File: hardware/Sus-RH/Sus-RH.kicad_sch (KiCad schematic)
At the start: 36 parts, among them J1 MX150_02x06_Vertical, J2 53307-2471, J3 Conn_01x03, J5 Conn_01x06, U1 TLV9002QDRQ1, U2 LDO40LPURY

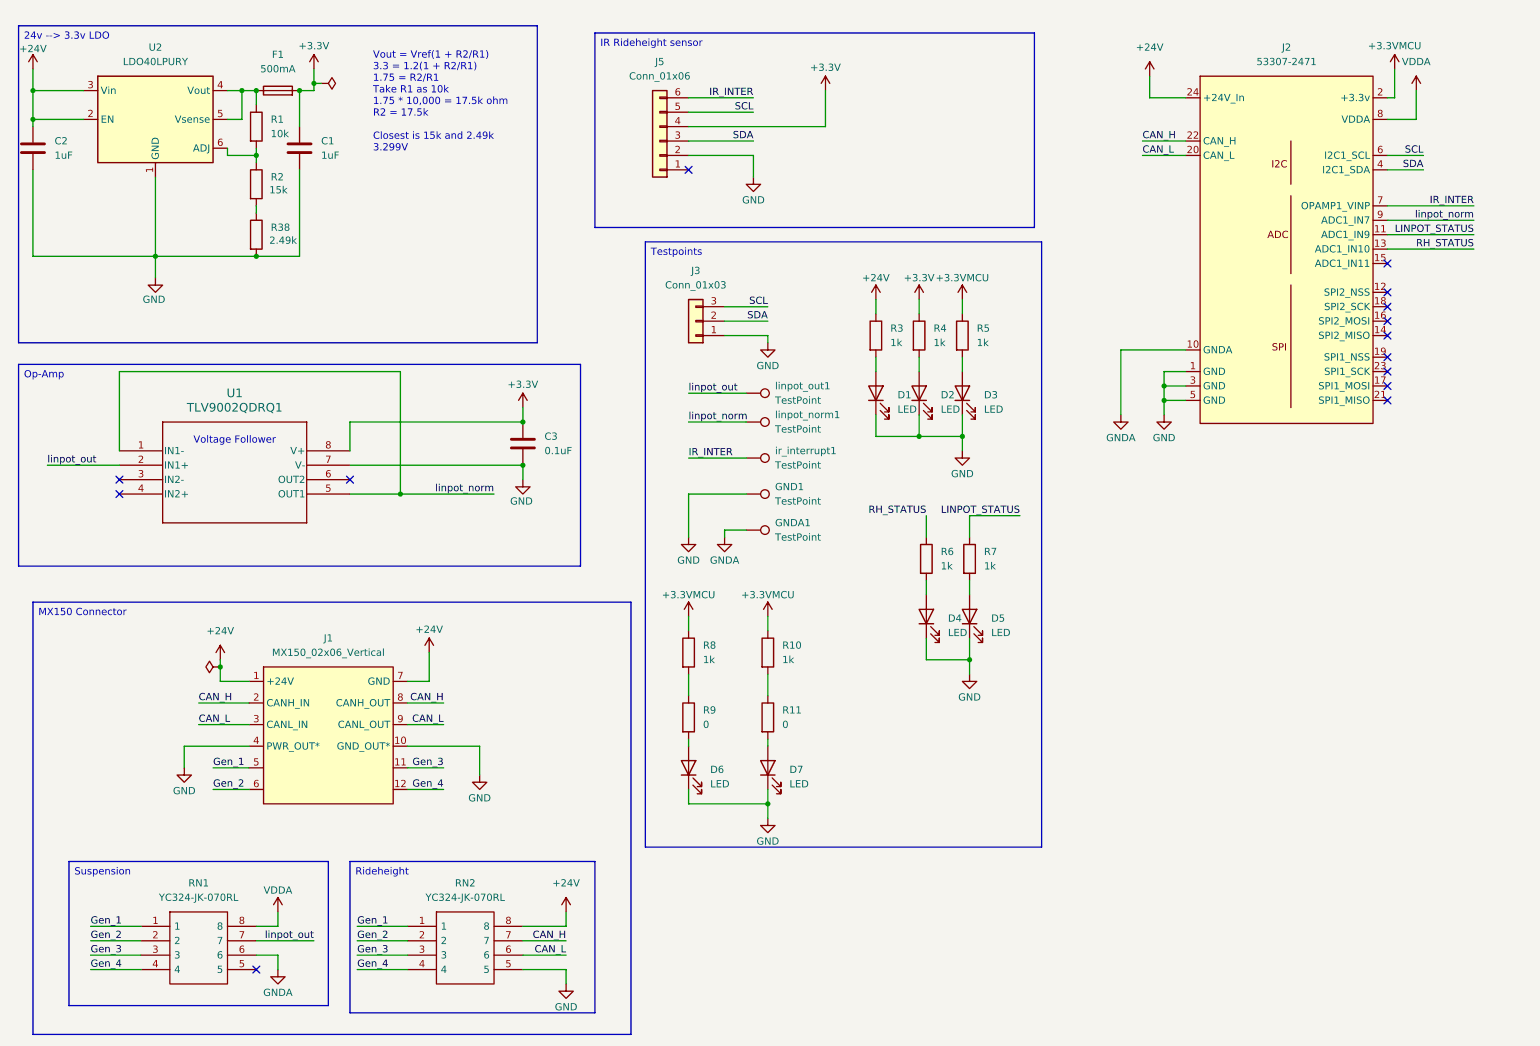
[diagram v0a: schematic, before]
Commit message: small changes, cubemx needs checking
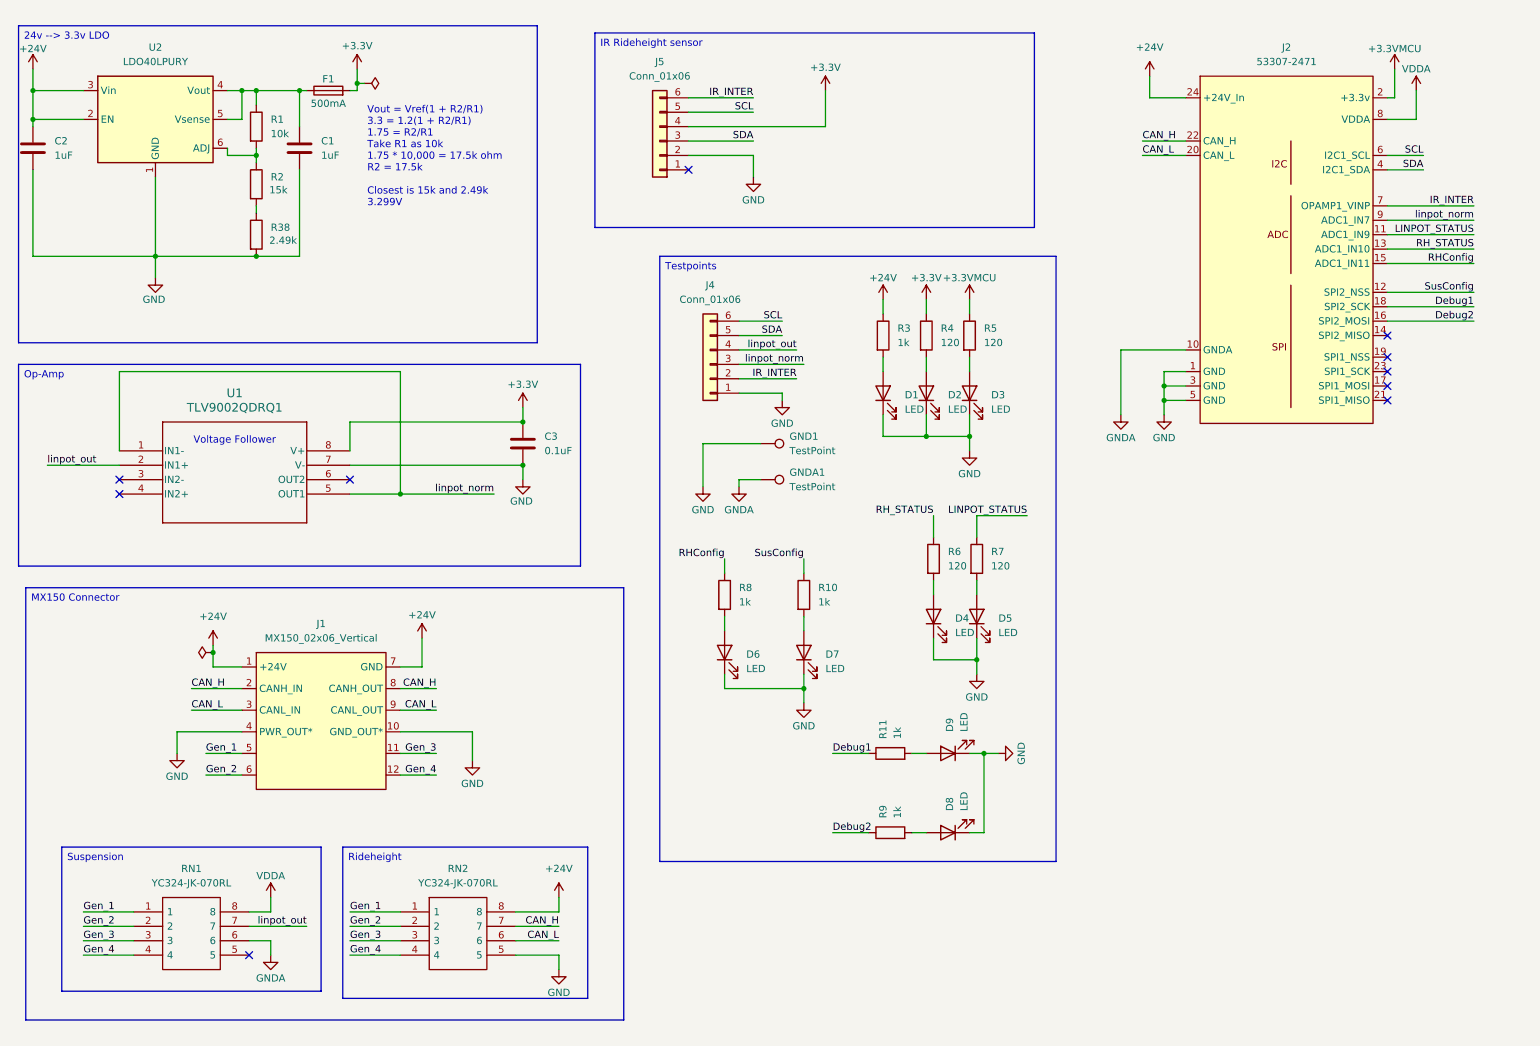
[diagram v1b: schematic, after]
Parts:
- removed J3: Conn_01x03, symbol Connector_Generic:Conn_01x03
- removed ir_interrupt1, linpot_norm1, linpot_out1: TestPoint, symbol Connector:TestPoint
- added D8, D9: LED, LED_SMD:LED_0603_1608Metric_Pad1.05x0.95mm_HandSolder, symbol Device:LED
- added J4: Conn_01x06, symbol Connector_Generic:Conn_01x06
- C3: footprint (none) -> Capacitor_SMD:C_0603_1608Metric_Pad1.08x0.95mm_HandSolder; P/N (none) -> MLASH168SB7104KTNA01
- D1, D2, D3, D4, D5, D6, D7: footprint (none) -> LED_SMD:LED_0603_1608Metric_Pad1.05x0.95mm_HandSolder; P/N (none) -> NCD0603R1
- GND1, GNDA1: footprint (none) -> TestPoint:TestPoint_Pad_1.0x1.0mm
- R10, R3, R8: footprint (none) -> Resistor_SMD:R_0603_1608Metric_Pad0.98x0.95mm_HandSolder; P/N (none) -> CRCW06031K00FKEI
- R11, R9: value 0 -> 1k; footprint (none) -> Resistor_SMD:R_0603_1608Metric_Pad0.98x0.95mm_HandSolder; P/N (none) -> CRCW06031K00FKEI
- R4, R5, R6, R7: value 1k -> 120; footprint (none) -> Resistor_SMD:R_0603_1608Metric_Pad0.98x0.95mm_HandSolder; P/N (none) -> CRCW06031K00FKEI
- RN1, RN2: footprint YC324JK07220RL -> 4pinRes:YC324JK07220RL; P/N (none) -> 603-YC324-JK-070RL
- U1: footprint SOIC8_D_TEX -> footprints:SOIC8_D_TEX; P/N (none) -> 595-TLV9002QDRQ1
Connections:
- net +3.3V: no longer C1.1
- net +3.3VMCU: no longer R10.1, R8.1
- net GND: now also D8.1 (K), D9.1 (K), J4.1 (Pin_1)
- net IR_INTER: now also J4.2 (Pin_2)
- net SCL: now also J4.6 (Pin_6)
- net SDA: now also J4.5 (Pin_5)
- net linpot_norm: now also J4.3 (Pin_3)
- net linpot_out: now also J4.4 (Pin_4)
- net at F1.1, R1.1, U2.4 (Vout)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: now also C1.1
- net at R8.2: now also D6.2 (A); no longer R9.1
- net at R9.2: now also D8.2 (A); no longer D6.2 (A)
- net at R10.2: now also D7.2 (A); no longer R11.1
- net at R11.2: now also D9.2 (A); no longer D7.2 (A)
- net SusConfig: now reaches J2.12 (SPI2_NSS)
- net SusConfig: now also R10.1
- net RHConfig: now reaches J2.15 (ADC1_IN11)
- net RHConfig: now also R8.1
- net Debug2: now reaches J2.16 (SPI2_MOSI)
- net Debug2: now also R9.1
- net Debug1: now reaches J2.18 (SPI2_SCK)
- net Debug1: now also R11.1
- no-connect marks 14 -> 10
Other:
- moved on the sheet: D1, D2, D3, D4, D5, D6, D7, F1, GND1, GNDA1, J1, R10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

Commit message: finished layout
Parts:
- J4: footprint (none) -> Connector_PinHeader_2.54mm:PinHeader_1x06_P2.54mm_Vertical
- J5: footprint Connector_Molex:Molex_Nano-Fit_105310-xx06_2x03_P2.50mm_Vertical -> Connector_Molex:Molex_Nano-Fit_105314-xx06_2x03_P2.50mm_Horizontal
- R3: value 1k -> 4.7k
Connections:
- net +24V: now also RN2.5; no longer RN2.8
- net GND: now also RN2.8; no longer RN2.5
- net Gen_1: now also RN2.4; no longer RN2.1
- net Gen_2: now also RN2.3; no longer RN2.2
- net Gen_3: now also RN2.2; no longer RN2.3
- net Gen_4: now also RN2.1; no longer RN2.4
- net CAN_H renamed CAN_+
- net CAN_+: now also RN2.6; no longer RN2.7
- net CAN_L renamed CAN_-
- net CAN_-: now also RN2.7; no longer RN2.6
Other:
- moved on the sheet: RN2

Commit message: fixed unity op-amp
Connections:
- net +3.3V: now also RN1.8; no longer C3.1, U1.8 (V+)
- net VDDA: now also C3.1, U1.8 (V+); no longer RN1.8
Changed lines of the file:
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@@
 			)
 		)
-		(property "Value" "VDDA"
+		(property "Value" "+3.3V"
 			(at 60.96 166.37 0)
 			(effects
@@
 			)
 		)
-		(property "Value" "+3.3V"
+		(property "Value" "VDDA"
 			(at 105.41 79.756 0)
 			(effects

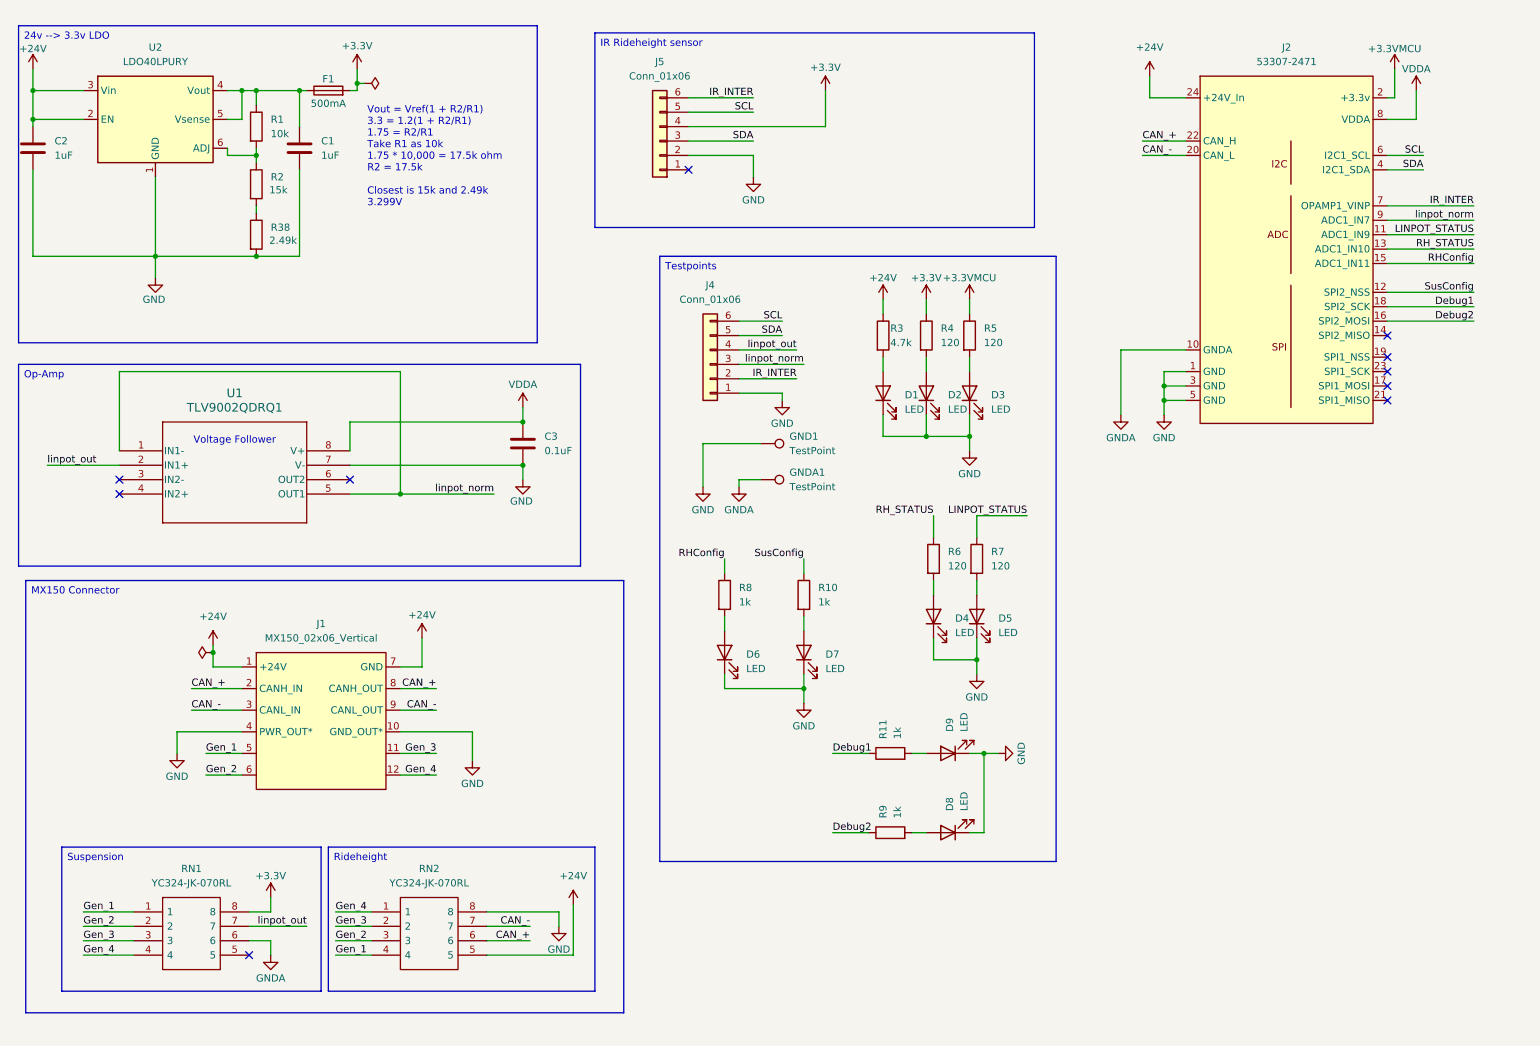
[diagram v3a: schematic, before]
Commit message: added silkscreen, fixed rh-sus layout rh-sus done
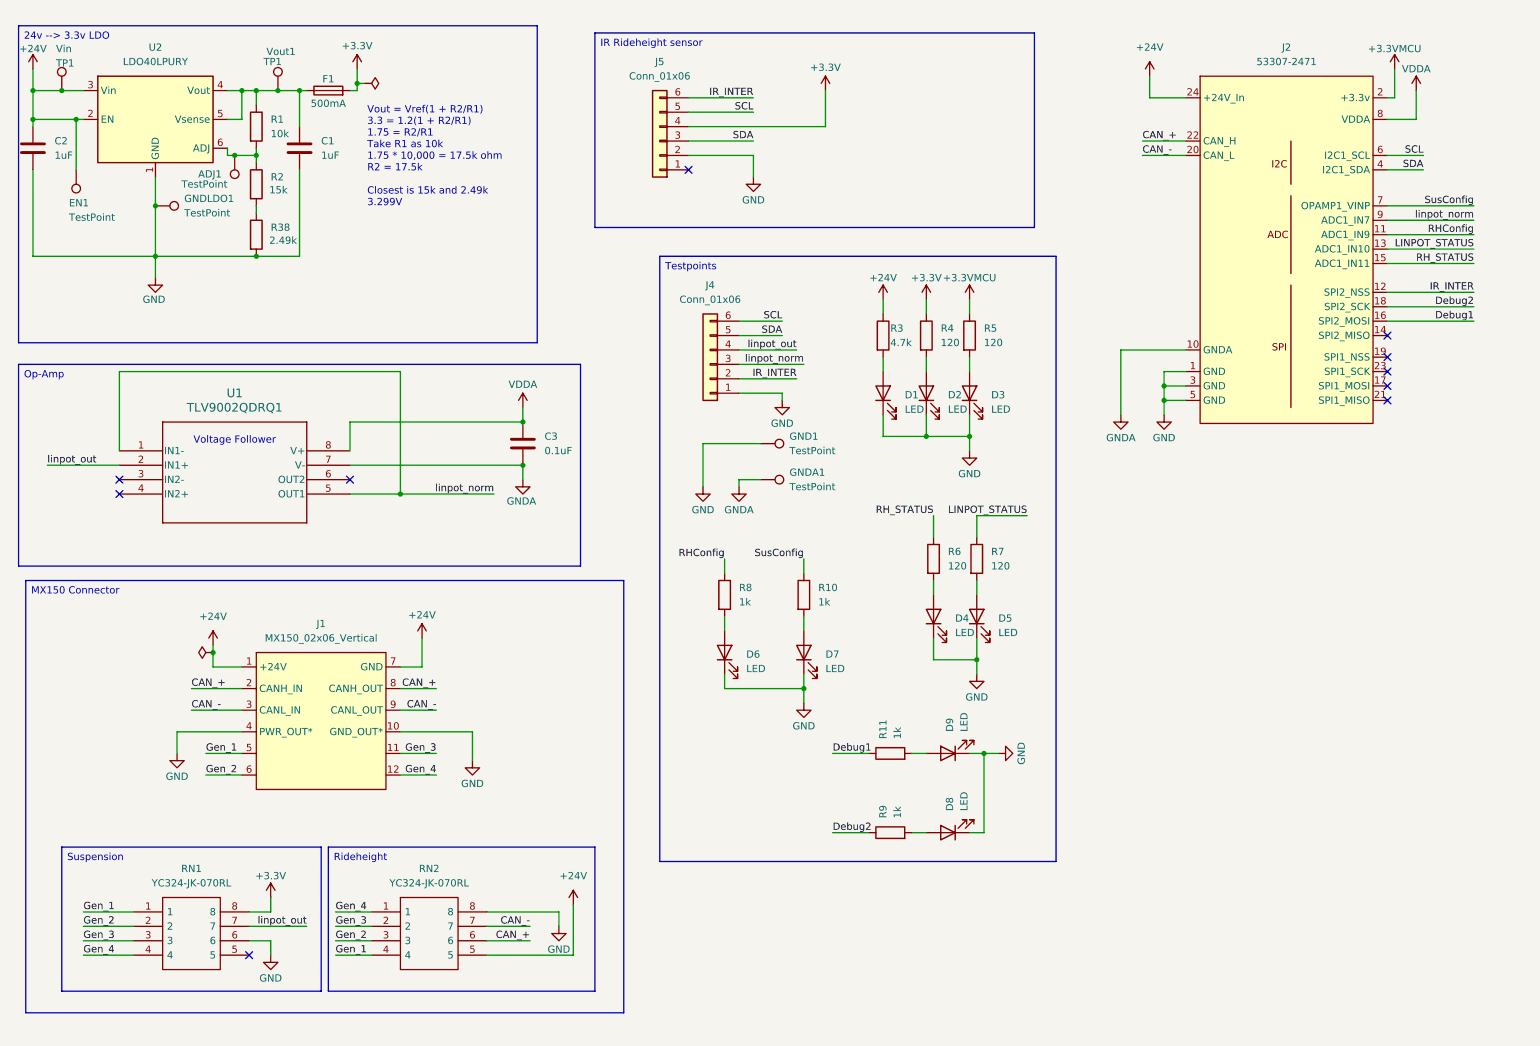
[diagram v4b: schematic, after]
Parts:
- added ADJ1, EN1, GNDLDO1: TestPoint, TestPoint:TestPoint_Pad_D1.0mm, symbol Connector:TestPoint
- added Vin, Vout1: TP1, TestPoint:TestPoint_Pad_D1.0mm, symbol Connector:TestPoint
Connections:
- net +24V: now also EN1.1, Vin.1
- net Debug1: now also J2.16 (SPI2_MOSI); no longer J2.18 (SPI2_SCK)
- net Debug2: now also J2.18 (SPI2_SCK); no longer J2.16 (SPI2_MOSI)
- net GND: now also RN1.6, GNDLDO1.1; no longer C3.2, U1.7 (V-)
- net GNDA: now also C3.2, U1.7 (V-); no longer RN1.6
- net IR_INTER: now also J2.12 (SPI2_NSS); no longer J2.7 (OPAMP1_VINP)
- net LINPOT_STATUS: now also J2.13 (ADC1_IN10); no longer J2.11 (ADC1_IN9)
- net RHConfig: now also J2.11 (ADC1_IN9); no longer J2.15 (ADC1_IN11)
- net RH_STATUS: now also J2.15 (ADC1_IN11); no longer J2.13 (ADC1_IN10)
- net SusConfig: now also J2.7 (OPAMP1_VINP); no longer J2.12 (SPI2_NSS)
- net at R1.2, R2.1, U2.6 (ADJ): now also ADJ1.1
- net at C1.1, F1.1, R1.1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: now also Vout1.1

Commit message: .bom files generated, cleaned up pitot board.
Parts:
- F1: P/N 534-3568 -> 3568
- J5: P/N 538-105310-1106 -> 105314-1106
- RN1, RN2: P/N 603-YC324-JK-070RL -> YC324-JK-070RL
- U1: P/N 595-TLV9002QDRQ1 -> TLV9002QDRQ1
- U2: P/N 511-LDO40LPU33RY -> LDO40LPURY
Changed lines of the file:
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@@
 			)
 		)
-		(property "P/N" "603-YC324-JK-070RL"
+		(property "P/N" "YC324-JK-070RL"
 			(at 36.83 172.72 0)
 			(effects
@@
 			)
 		)
-		(property "P/N" "595-TLV9002QDRQ1"
+		(property "P/N" "TLV9002QDRQ1"
 			(at 34.29 91.44 0)
 			(effects
@@
 			)
 		)
-		(property "P/N" "603-YC324-JK-070RL"
+		(property "P/N" "YC324-JK-070RL"
 			(at 78.74 172.72 0)
 			(effects
@@
 			)
 		)
-		(property "P/N" "511-LDO40LPU33RY"
+		(property "P/N" "LDO40LPURY"
 			(at 40.64 33.02 0)
 			(effects
@@
 			)
 		)
-		(property "P/N" "538-105310-1106"
+		(property "P/N" "105314-1106 "
 			(at 129.54 36.83 0)
 			(effects
@@
 			)
 		)
-		(property "P/N" "534-3568"
+		(property "P/N" "3568"
 			(at 71.12 27.94 90)
 			(effects
